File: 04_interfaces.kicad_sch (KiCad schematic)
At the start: 33 parts, among them J4 TFT-H035B22WVIST8N20_V3-0, J5 MicroSD, Q3 AO3401A, SW1 UP, SW2 DOWN, SW3 OK, SW4 BACK, U7 TPS61169DCKR, U8 TPS22918DBVR

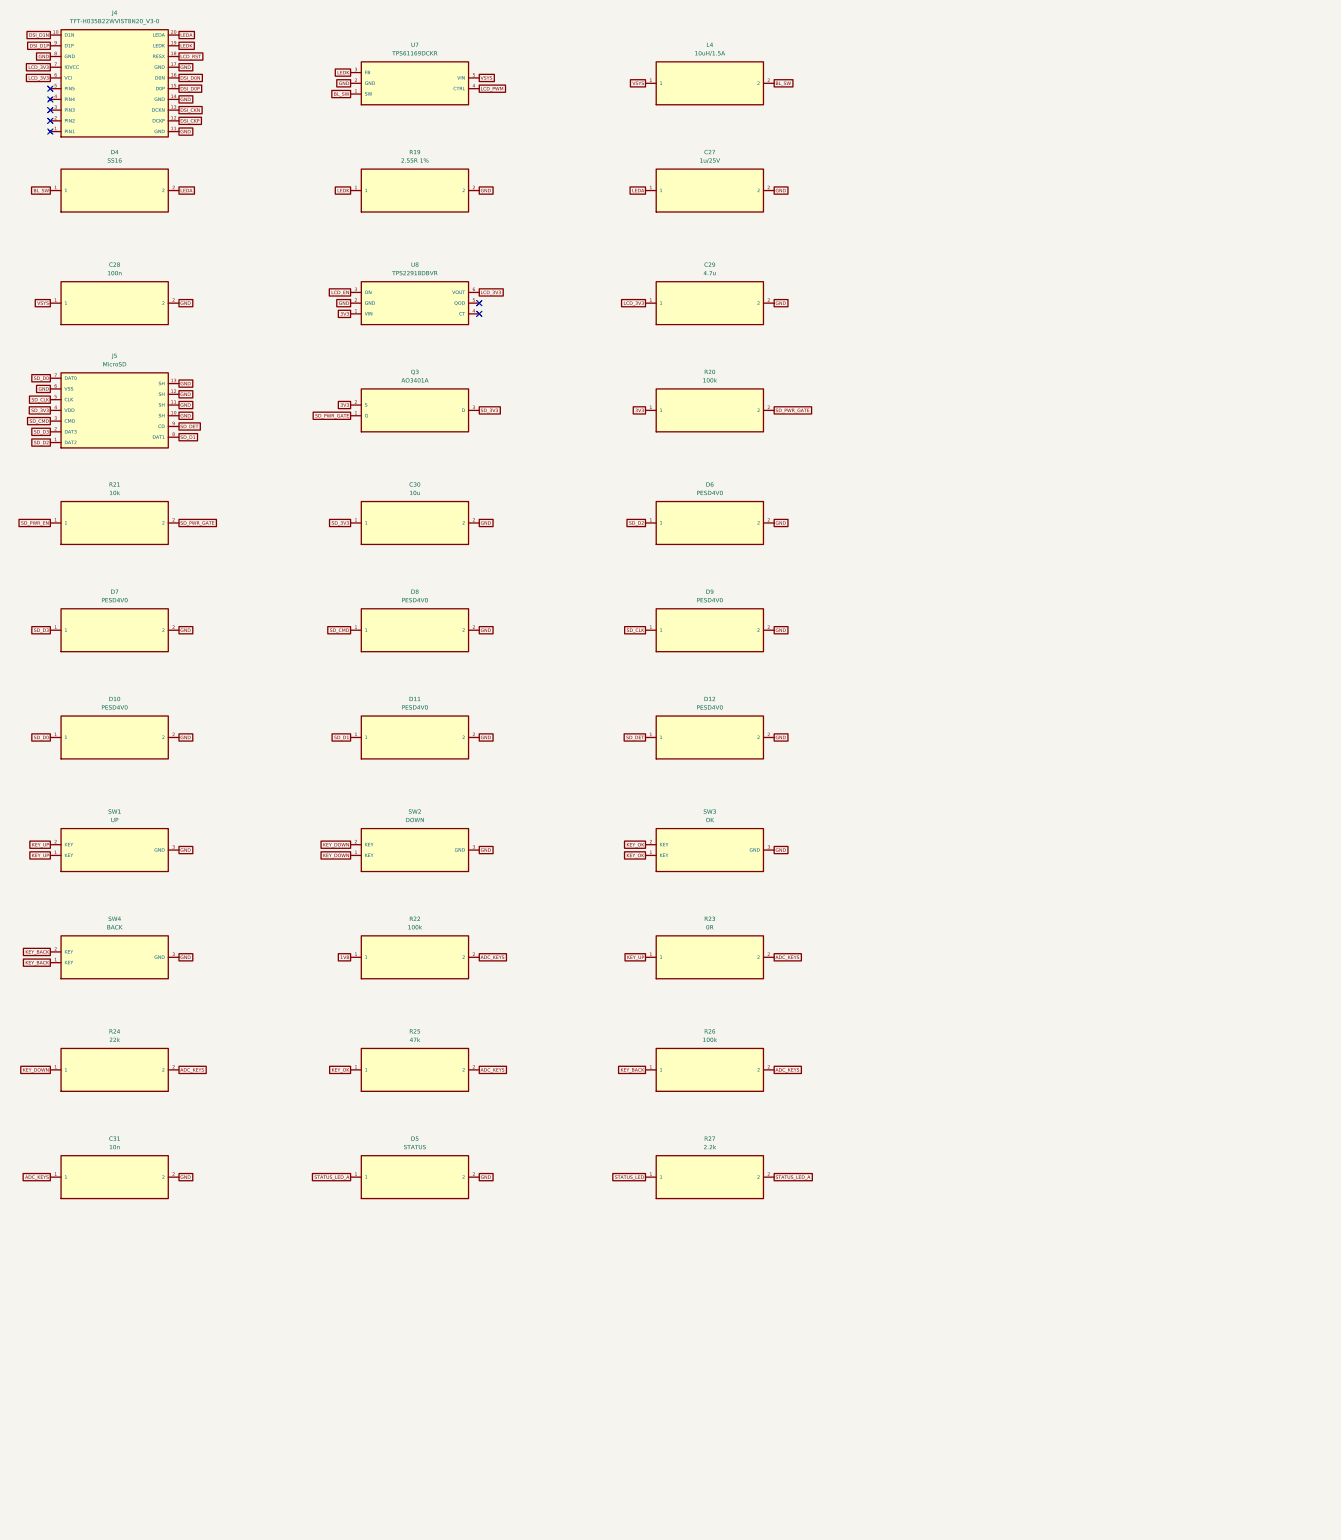
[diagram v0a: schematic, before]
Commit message: feat(display): wire KD024 45-pin MIPI1 on J4; DNP TFT backlight; EL nets TBD
- Replace FPC20 TFT placeholder with Molex 502598-4591 / KD024EGOIN152-01
- IM0/IM1→GND; VCI via U8; VDDIO from 1V8; TE on PD20; DSI lane0 only
- ELVDD/ELVSS/SWIRE nets + probe pads; no invented EL PMIC
- U7 backlight chain DNP; docs/DISPLAY_KD024_NETMAP.md; gates in_progress
- fabrication_released remains false
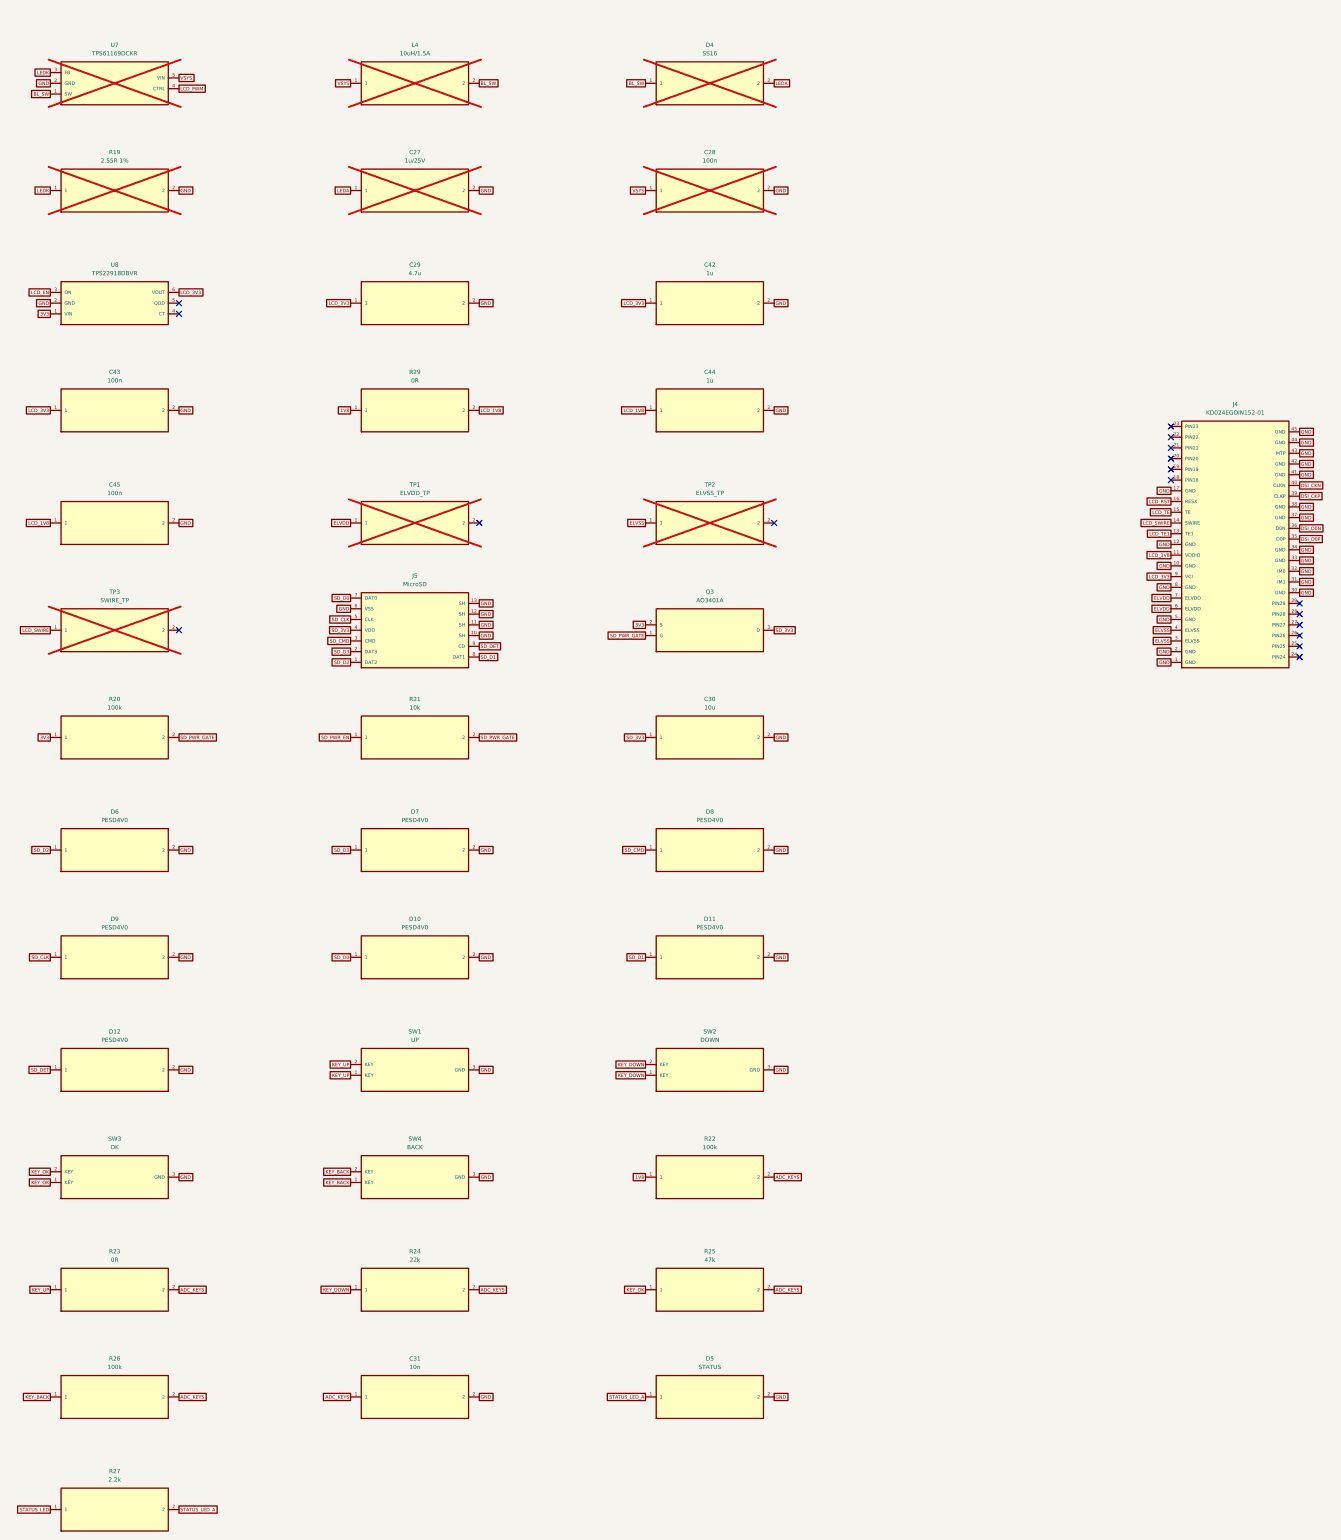
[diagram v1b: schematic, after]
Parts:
- added C42: 1u, Sameat:0603, symbol Sameat:C42_1u
- added C43: 100n, Sameat:0402, symbol Sameat:C43_100n
- added C44: 1u, Sameat:0603, symbol Sameat:C44_1u
- added C45: 100n, Sameat:0402, symbol Sameat:C45_100n
- added R29: 0R, Sameat:0402, symbol Sameat:R29_0R
- added TP1: ELVDD_TP, Sameat:0402, symbol Sameat:TP1_ELVDD_TP
- added TP2: ELVSS_TP, Sameat:0402, symbol Sameat:TP2_ELVSS_TP
- added TP3: SWIRE_TP, Sameat:0402, symbol Sameat:TP3_SWIRE_TP
- C27, C28, D4, L4, R19, U7: now not fitted
- J4: value TFT-H035B22WVIST8N20_V3-0 -> KD024EGOIN152-01; footprint Sameat:FPC20 -> Sameat:FPC45; symbol Sameat:J4_TFT-H035B22WVIST8N20_V3-0 -> Sameat:J4_KD024EGOIN152-01; LCSC C596730 -> (none); MPN FH12-20S-0.5SH(55) -> 502598-4591
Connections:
- net DSI_D1N is gone; now on net GND: J4.10 (GND)
- net DSI_D1P is gone; now on net LCD_3V3: J4.9 (VCI)
- net 1V8: now also R29.1
- net DSI_CKN: now also J4.40 (CLKN); no longer J4.13 (DCKN)
- net DSI_CKP: now also J4.39 (CLKP); no longer J4.12 (DCKP)
- net DSI_D0N: now also J4.36 (D0N); no longer J4.16 (D0N)
- net DSI_D0P: now also J4.35 (D0P); no longer J4.15 (D0P)
- net GND: now also J4.1 (GND), J4.12 (GND), J4.2 (GND), J4.30 (GND), J4.31 (IM1), J4.32 (IM0), J4.33 (GND), J4.34 (GND), J4.37 (GND), J4.38 (GND), J4.41 (GND), J4.42 (GND), J4.43 (MTP), J4.44 (GND), J4.45 (GND), J4.5 (GND), C42.2, C43.2, C44.2, C45.2; no longer J4.11 (GND), J4.14 (GND)
- net LCD_3V3: now also C42.1, C43.1; no longer J4.6 (VCI), J4.7 (IOVCC)
- net LCD_RST: now also J4.16 (RESX); no longer J4.18 (RESX)
- net LEDA: no longer J4.20 (LEDA)
- net LEDK: no longer J4.19 (LEDK)
- net ELVSS: now reaches J4.3 (ELVSS)
- net ELVSS: now also J4.4 (ELVSS), TP2.1
- new net ELVDD: J4.6 (ELVDD), J4.7 (ELVDD), TP1.1
- new net LCD_1V8: C44.1, C45.1, J4.11 (VDDIO), R29.2
- new net LCD_SWIRE: J4.14 (SWIRE), TP3.1
- new net LCD_TE: J4.15 (TE)
- new net LCD_TE1: J4.13 (TE1)
- no-connect marks 7 -> 17
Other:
- moved on the sheet: C29, C30, C31, D10, D11, D12, D5, D6, D7, D8, D9, J5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

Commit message: feat(display): add TPS65631 EL± bias (C165127) for KD024
- Lock EL PMIC to TPS65631DPDR: ELVDD/ELVSS, CTRL=LCD_EN
- Defaults 4.6V / -4.0V (within KD024 abs max); panel SWIRE optional via R31 DNP
- Passives per TI typical app; docs/DISPLAY_EL_TPS65631.md
- fabrication_released remains false
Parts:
- removed TP1: ELVDD_TP, Sameat:0402, symbol Sameat:TP1_ELVDD_TP
- removed TP2: ELVSS_TP, Sameat:0402, symbol Sameat:TP2_ELVSS_TP
- removed TP3: SWIRE_TP, Sameat:0402, symbol Sameat:TP3_SWIRE_TP
- added C46: 10u, Sameat:0603, symbol Sameat:C46_10u
- added C47: 10u, Sameat:0603, symbol Sameat:C47_10u
- added C48: 10u, Sameat:0603, symbol Sameat:C48_10u
- added C49: 10u, Sameat:0603, symbol Sameat:C49_10u
- added C50: 10u, Sameat:0603, symbol Sameat:C50_10u
- added C51: 100n, Sameat:0402, symbol Sameat:C51_100n
- added L5: 4.7uH, Sameat:IND_2x2, symbol Sameat:L5_4.7uH
- added L6: 4.7uH, Sameat:IND_2x2, symbol Sameat:L6_4.7uH
- added R31: 0R, Sameat:0402, symbol Sameat:R31_0R
- added U10: TPS65631DPDR, Sameat:WSON-12, symbol Sameat:U10_TPS65631DPDR
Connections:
- net ELVDD: now also C48.1, U10.3 (OUTP), U10.4 (FBS)
- net ELVSS: now also C49.1, C50.1, U10.9 (OUTN)
- net GND: now also C46.2, C47.2, C48.2, C49.2, C50.2, C51.2, L6.2, U10.13 (EPAD), U10.2 (PGND), U10.5 (AGND), U10.6 (GND)
- net LCD_EN: now also R31.2, U10.7 (CTRL)
- net LCD_SWIRE: now also R31.1
- net VSYS: now also C46.1, C47.1, L5.1, U10.11 (AVIN), U10.12 (PVIN)
- new net EL_CT: C51.1, U10.8 (CT)
- new net EL_SWN: L6.1, U10.10 (SWN)
- new net EL_SWP: L5.2, U10.1 (SWP)
- no-connect marks 17 -> 14
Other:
- moved on the sheet: C30, C31, D10, D11, D12, D5, D6, D7, D8, D9, J5, Q3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

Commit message: gpt6-codex
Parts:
- removed C27: 1u/25V, Sameat:0603, symbol Sameat:C27_1u/25V
- removed C28: 100n, Sameat:0402, symbol Sameat:C28_100n
- removed D4: SS16, Sameat:D_SOD123, symbol Sameat:D4_SS16
- removed L4: 10uH/1.5A, Sameat:IND_2x2, symbol Sameat:L4_10uH/1.5A
- removed R19: 2.55R 1%, Sameat:0603, symbol Sameat:R19_2.55R 1%
- removed U7: TPS61169DCKR, Sameat:SC70-5, symbol Sameat:U7_TPS61169DCKR
- J4: MPN 502598-4591 -> 502598-4593
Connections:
- net GND: now also J4.MP1 (MOUNT), J4.MP2 (MOUNT)
- net LCD_TE1: no longer names the net of J4.13 (TE1)
- no-connect marks 14 -> 15
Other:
- moved on the sheet: C29, C30, C31, C42, C43, C44, C45, C46, C47, C48, C49, C50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
